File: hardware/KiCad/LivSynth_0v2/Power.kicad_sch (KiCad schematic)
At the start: 40 parts, among them J5 Barrel_Jack_Switch, SW6 SW_SPDT, U1 TL074, U3 TL074, U4 TL074, U5 LM1117-3.3, U6 TL074, U7 LM13700, U8 TL074

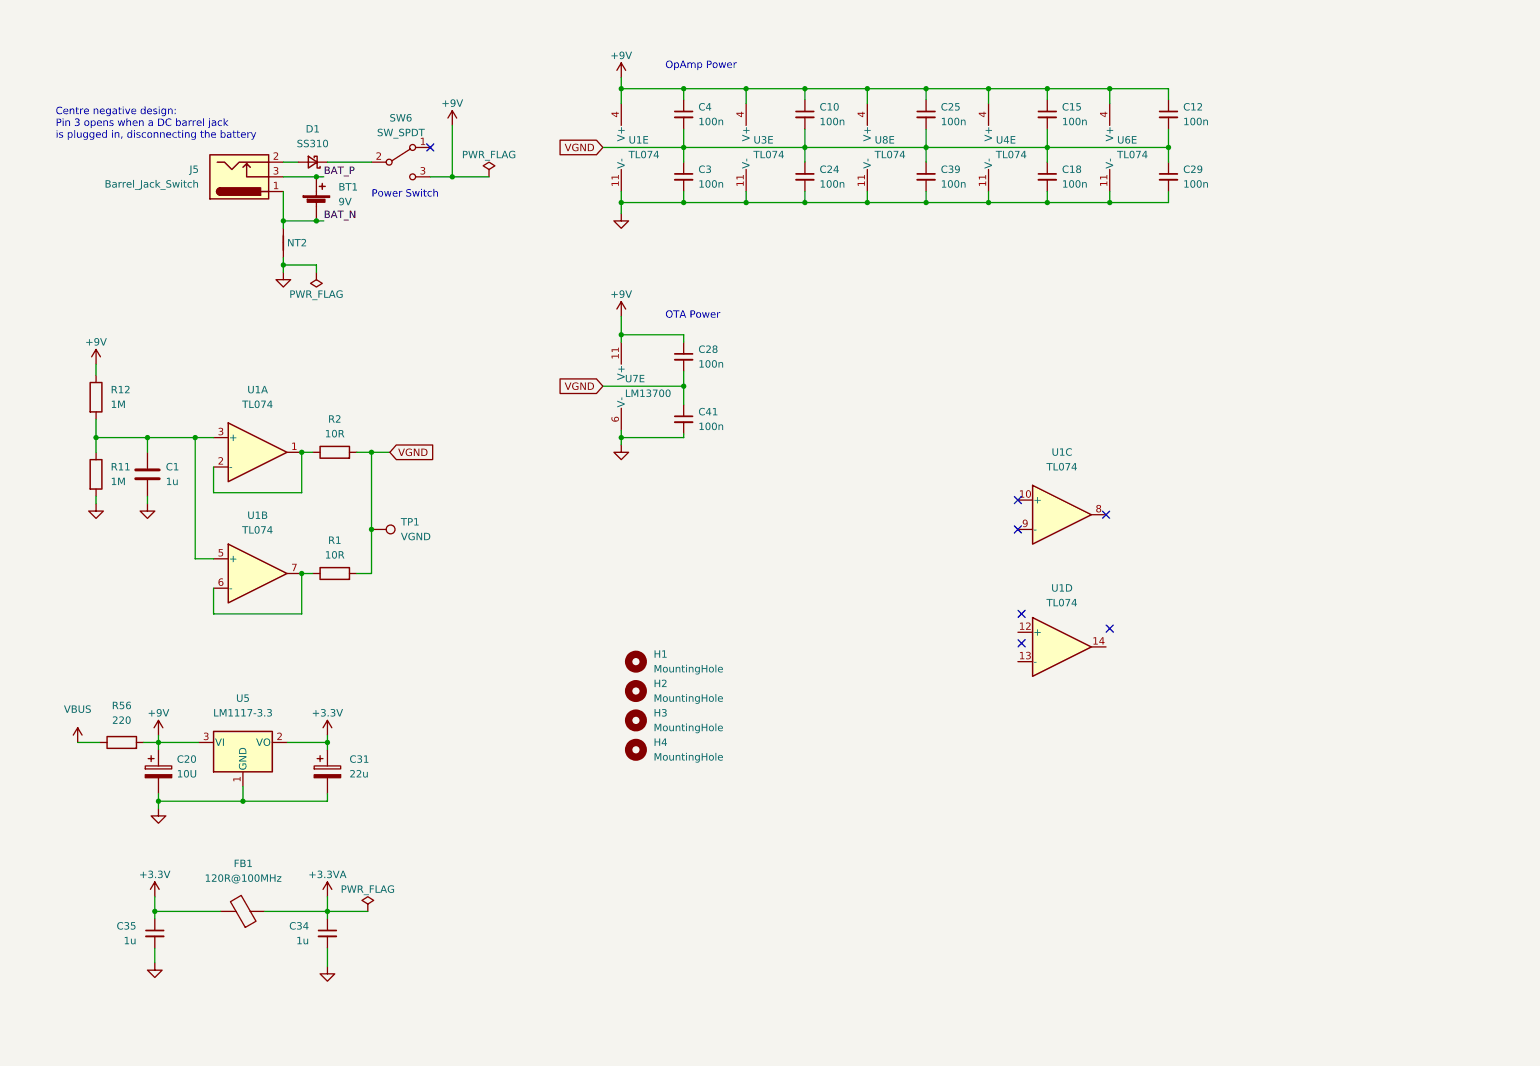
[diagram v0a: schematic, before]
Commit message: Analog redesign:  - Power: Add voltage and current test points  - MCU: use PA11/PA12 for USB DFU interface  - MCU: add NRST reset switch  - Slew: increase portamento cap  - VCO: invert trim pots  - VCF: let resonance kick in earlier  - VCF: invert pots  - VCA: invert trim pot  - EG: full redesign, properly referencing VGND now  - LFO: R61 = 51K  - ModMatrix: add EG attenuverters  - IO: invert pots  - IO: limit output gain for 1W speaker  - IO: connect BTN_SHIFT in gap free order to SR
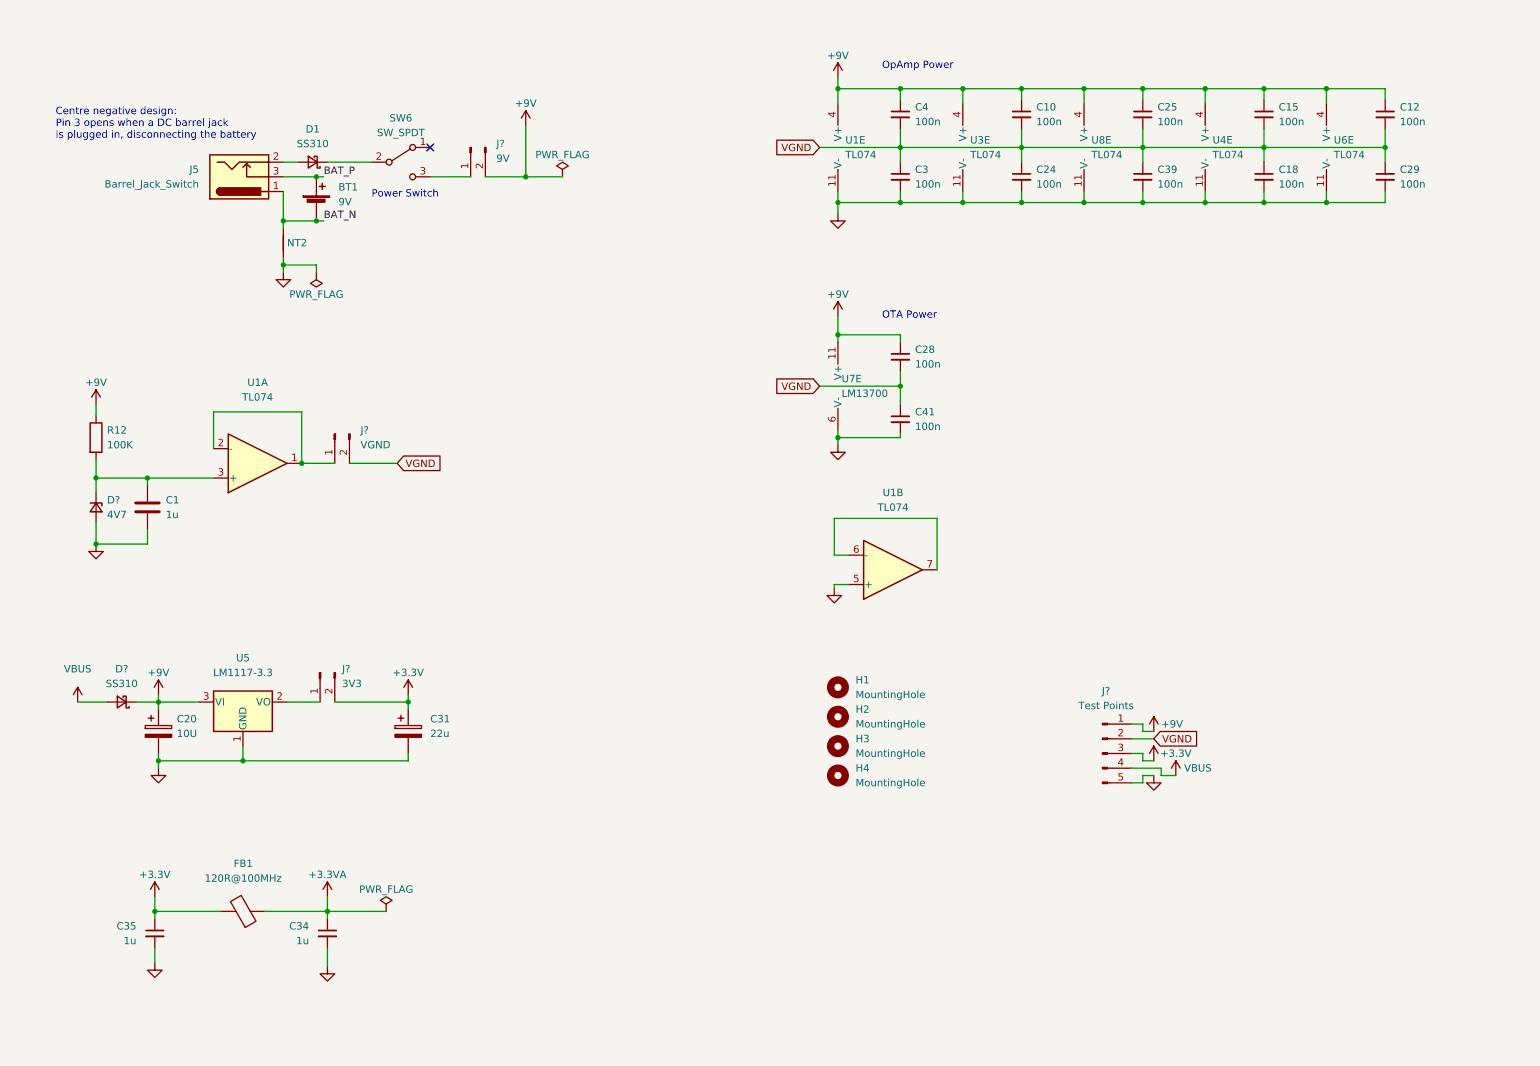
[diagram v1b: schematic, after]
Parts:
- removed R1, R2: 10R, Resistor_THT:R_Axial_DIN0207_L6.3mm_D2.5mm_P7.62mm_Horizontal, symbol Device:R
- removed R11: 1M, Resistor_THT:R_Axial_DIN0207_L6.3mm_D2.5mm_P7.62mm_Horizontal, symbol Device:R
- removed R56: 220, Resistor_THT:R_Axial_DIN0207_L6.3mm_D2.5mm_P7.62mm_Horizontal, symbol Device:R
- removed TP1: VGND, Connector_PinHeader_2.54mm:PinHeader_1x01_P2.54mm_Vertical, symbol Connector:TestPoint
- removed unit 3 of U1
- removed unit 4 of U1
- added D?: SS310, Diode_SMD:D_SMC_Handsoldering, symbol Device:D_Schottky_Small
- added D?: 4V7, symbol Device:D_Zener_Small
- added J?: 9V, Connector_PinHeader_2.54mm:PinHeader_1x02_P2.54mm_Vertical, symbol Connector:Conn_01x02_Male
- added J?: VGND, Connector_PinHeader_2.54mm:PinHeader_1x02_P2.54mm_Vertical, symbol Connector:Conn_01x02_Male
- added J?: Test Points, symbol Connector:Conn_01x05_Male
- added J?: 3V3, Connector_PinHeader_2.54mm:PinHeader_1x02_P2.54mm_Vertical, symbol Connector:Conn_01x02_Male
- R12: value 1M -> 100K
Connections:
- net +3.3V: now also J?.2 (Pin_2), J?.3 (Pin_3); no longer U5.2 (VO)
- net +9V: now also D?.1 (K), J?.1 (Pin_1), J?.2 (Pin_2); no longer SW6.3 (C)
- net GND: now also U1.5 (+), D?.2 (A), J?.5 (Pin_5)
- net VBUS: now also D?.2 (A), J?.4 (Pin_4)
- net VGND: now also J?.2 (Pin_2), J?.2 (Pin_2)
- net at C1.1, R12.2, U1.3 (+): now also D?.1 (K); no longer U1.5 (+)
- net at U1.1, U1.2 (-): now also J?.1 (Pin_1)
- new net: J?.1 (Pin_1), U5.2 (VO)
- new net: J?.1 (Pin_1), SW6.3 (C)
- no-connect marks 7 -> 1
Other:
- moved on the sheet: C1, C10, C12, C15, C18, C20, C24, C25, C28, C29, C3, C31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

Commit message: Analog Redesign:  - Power: Build ververse polarity protection using P-Mosfet and Zener Diode      - (https://www.youtube.com/watch?v=Ltx4vovY5Z4 - 1:28)  - Power: Build adjustable buck regulator for 8-9V stable voltage source  - PCB: Add location for order number ("JLCJLCJLCJLC")  - General: Add Tooling Holes for PCB assembly  - PCB: check frontend component layout for symmetry  - VCF: fix sound issues  - PCB: Add SloBlo icon  - PCB: Add switch labels to front side  - EG: test new design  - MCU: Add some debug pins
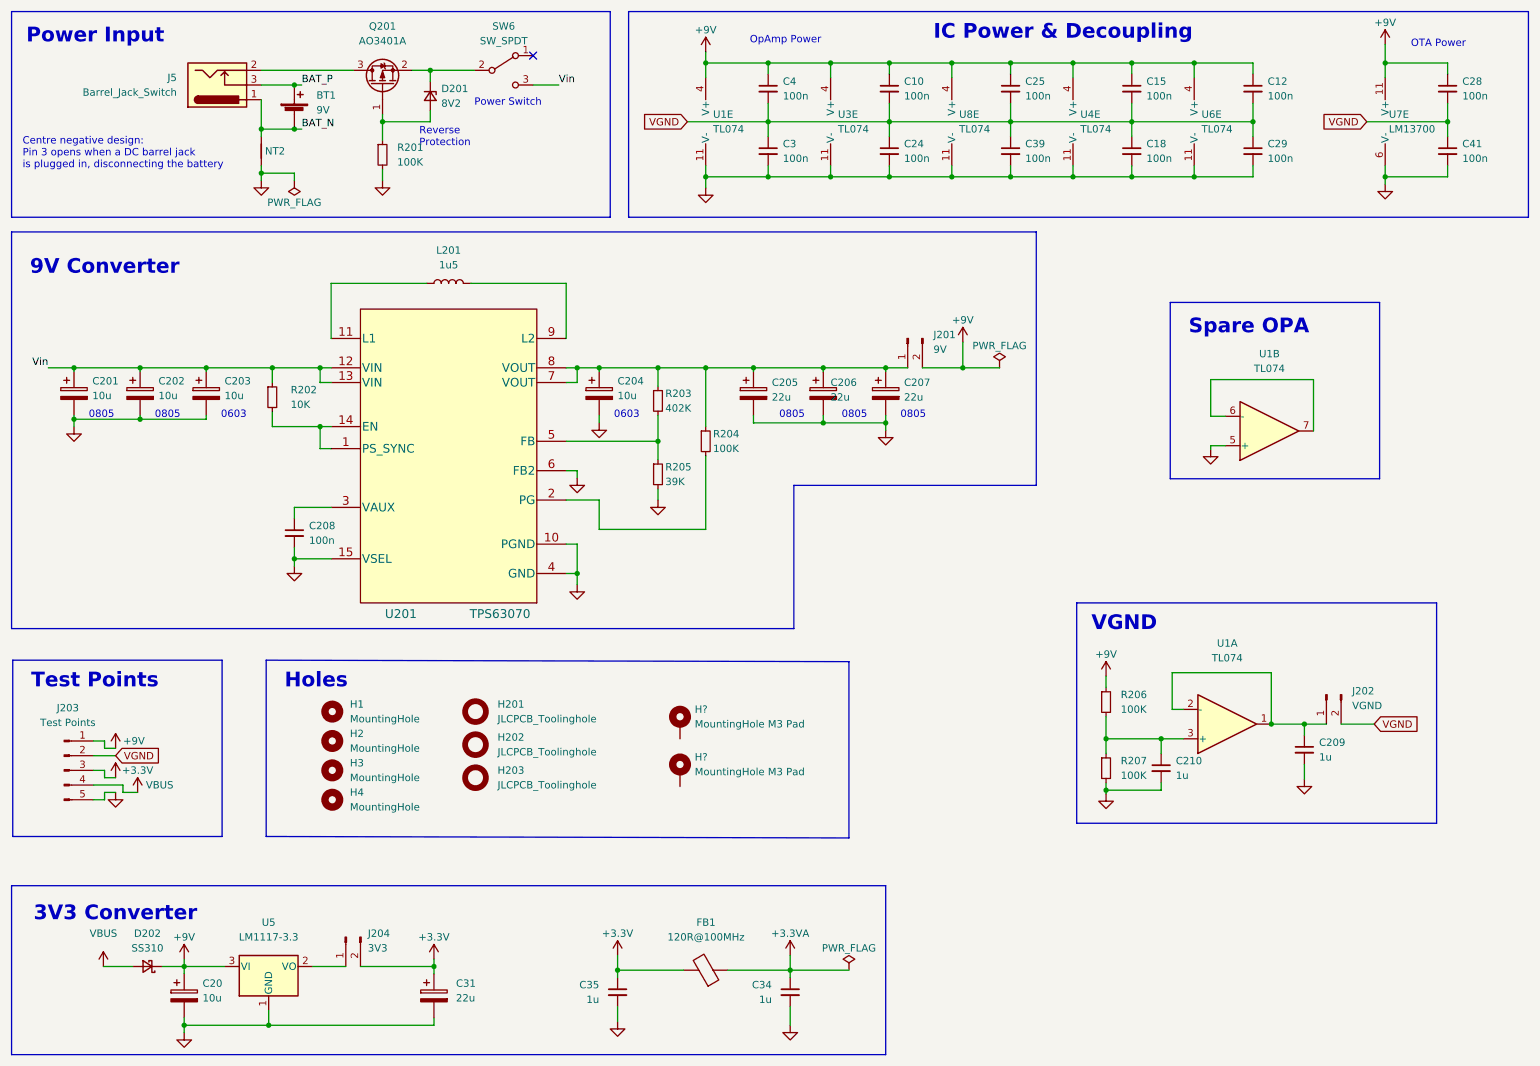
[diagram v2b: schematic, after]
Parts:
- removed C1: 1u, Capacitor_THT:C_Rect_L7.2mm_W5.5mm_P5.00mm_FKS2_FKP2_MKS2_MKP2, symbol Device:C
- removed D1: SS310, Diode_SMD:D_SMC_Handsoldering, symbol Device:D_Schottky_Small
- removed D?: 4V7, symbol Device:D_Zener_Small
- removed J?: 9V, Connector_PinHeader_2.54mm:PinHeader_1x02_P2.54mm_Vertical, symbol Connector:Conn_01x02_Male
- removed R12: 100K, Resistor_THT:R_Axial_DIN0207_L6.3mm_D2.5mm_P7.62mm_Horizontal, symbol Device:R
- added C201, C202, C203, C204: 10u, Capacitor_THT:CP_Radial_D8.0mm_P3.50mm, symbol Device:C_Polarized
- added C205, C206, C207: 22u, Capacitor_THT:CP_Radial_D8.0mm_P3.50mm, symbol Device:C_Polarized
- added C208: 100n, Capacitor_THT:C_Rect_L7.2mm_W2.5mm_P5.00mm_FKS2_FKP2_MKS2_MKP2, symbol Device:C_Small
- added C209, C210: 1u, symbol Device:C_Small
- added D201: 8V2, Diode_SMD:D_SOD-123, symbol Device:D_Zener_Small
- added H201, H202, H203: JLCPCB_Toolinghole, symbol SloBlo:JLCPCB_Toolinghole
- added H? (x2): MountingHole M3 Pad, symbol Mechanical:MountingHole_Pad
- added J201: 9V, Connector_PinHeader_2.54mm:PinHeader_1x02_P2.54mm_Vertical, symbol Connector:Conn_01x02_Male
- added L201: 1u5, symbol Device:L
- added Q201: AO3401A, Package_TO_SOT_SMD:SOT-23, symbol Transistor_FET:AO3401A
- added R201, R204, R206, R207: 100K, symbol Device:R_Small
- added R202: 10K, symbol Device:R_Small
- added R203: 402K, symbol Device:R_Small
- added R205: 39K, symbol Device:R_Small
- added U201: TPS63070, RNM0015A, symbol SloBlo:TPS63070x
- C20: value 10U -> 10u
- U1, U3, U4, U6, U8: LCSC (none) -> C2057504
- U5: LCSC (none) -> C126027
- U7: LCSC (none) -> C4370932
- gave numbers to parts that had none: 4
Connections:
- net +9V: now also J201.2 (Pin_2), R206.1
- net GND: now also C201.2, C202.2, C203.2, C204.2, C205.2, C206.2, C207.2, C208.2, C209.2, C210.2, R201.2, R205.2, R207.2, U201.10 (PGND), U201.15 (VSEL), U201.4 (GND), U201.6 (FB2)
- net at J5.2: now also Q201.3 (D)
- net at SW6.2 (B): now also D201.1 (K), Q201.2 (S)
- net Vin: now reaches SW6.3 (C)
- net Vin: now also C201.1, C202.1, C203.1, R202.1, U201.12 (VIN), U201.13 (VIN)
- net at J202.1 (Pin_1), U1.1, U1.2 (-): now also C209.1
- net at U1.3 (+): now also C210.1, R206.2, R207.1
- new net: C204.1, C205.1, C206.1, C207.1, J201.1 (Pin_1), R203.1, R204.1, U201.7 (VOUT), U201.8 (VOUT)
- new net: D201.2 (A), Q201.1 (G), R201.1
- new net: R202.2, U201.1 (PS_SYNC), U201.14 (EN)
- new net: L201.1, U201.11 (L1)
- new net: R204.2, U201.2 (PG)
- new net: C208.1, U201.3 (VAUX)
- new net: R203.2, R205.1, U201.5 (FB)
- new net: L201.2, U201.9 (L2)
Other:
- note added: "0603"
- note added: "0805"
- note added: "3V3 Converter"
- note added: "9V Converter"
- note added: "Holes"
- note added: "IC Power & Decoupling"
- note added: "Power Input"
- note added: "Reverse Protection"
- note added: "Spare OPA"
- note added: "Test Points"
- note added: "VGND"
- moved on the sheet: BT1, C10, C12, C15, C18, C20, C24, C25, C28, C29, C3, C31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

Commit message: progress 2023-01-21
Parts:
- removed H? (x2): MountingHole M3 Pad, symbol Mechanical:MountingHole_Pad
- C201, C202, C205, C206, C207: footprint Capacitor_THT:CP_Radial_D8.0mm_P3.50mm -> Capacitor_SMD:C_0805_2012Metric_Pad1.18x1.45mm_HandSolder
- C203, C204: footprint Capacitor_THT:CP_Radial_D8.0mm_P3.50mm -> Capacitor_SMD:C_0603_1608Metric_Pad1.08x0.95mm_HandSolder
- C209, C210: footprint (none) -> Capacitor_THT:C_Rect_L7.2mm_W5.5mm_P5.00mm_FKS2_FKP2_MKS2_MKP2
- H201, H202, H203: footprint (none) -> SloBlo:JLCPCB_ToolingHole
- J203: footprint (none) -> Connector_PinHeader_2.54mm:PinHeader_1x06_P2.54mm_Vertical; symbol Connector:Conn_01x05_Male -> Connector:Conn_01x06_Male
- L201: footprint (none) -> Inductor_SMD:L_Sunlord_SWPA5020S
- NT2: footprint NetTie:NetTie-2_SMD_Pad2.0mm -> NetTie:NetTie-2_SMD_Pad0.5mm
- R201, R206, R207: footprint (none) -> Resistor_THT:R_Axial_DIN0207_L6.3mm_D2.5mm_P7.62mm_Horizontal
- R202, R203, R204, R205: footprint (none) -> Resistor_SMD:R_0603_1608Metric_Pad0.98x0.95mm_HandSolder
- U201: footprint RNM0015A -> SloBlo:TPS63070x
- U5: footprint Package_TO_SOT_SMD:SOT-223 -> Package_TO_SOT_SMD:SOT-223-3_TabPin2
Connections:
- net +3.3V: no longer C31.1
- net +3.3VA: now also J203.4 (Pin_4)
- net GND: now also J203.6 (Pin_6); no longer J203.5 (Pin_5)
- net VBUS: now also J203.5 (Pin_5); no longer J203.4 (Pin_4)
- net Vout: now reaches C204.1, C205.1, C206.1, C207.1, J201.1 (Pin_1), R203.1, R204.1, U201.7 (VOUT), U201.8 (VOUT)
- net VGREF: now reaches C210.1, R206.2, R207.1, U1.3 (+)
- net at J204.1 (Pin_1), U5.2 (VO): now also C31.1
- net L1: now reaches L201.1, U201.11 (L1)
- net PG: now reaches R204.2, U201.2 (PG)
- net Vaux: now reaches C208.1, U201.3 (VAUX)
- net FB: now reaches R203.2, R205.1, U201.5 (FB)
- net L2: now reaches L201.2, U201.9 (L2)
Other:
- moved on the sheet: C10, C12, C15, C18, C24, C25, C28, C29, C3, C31, C39, C4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
